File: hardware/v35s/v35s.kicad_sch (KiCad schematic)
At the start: 13 parts, among them J1 nuMezzanine_4x34, U1 uPD70337L-8-xxx

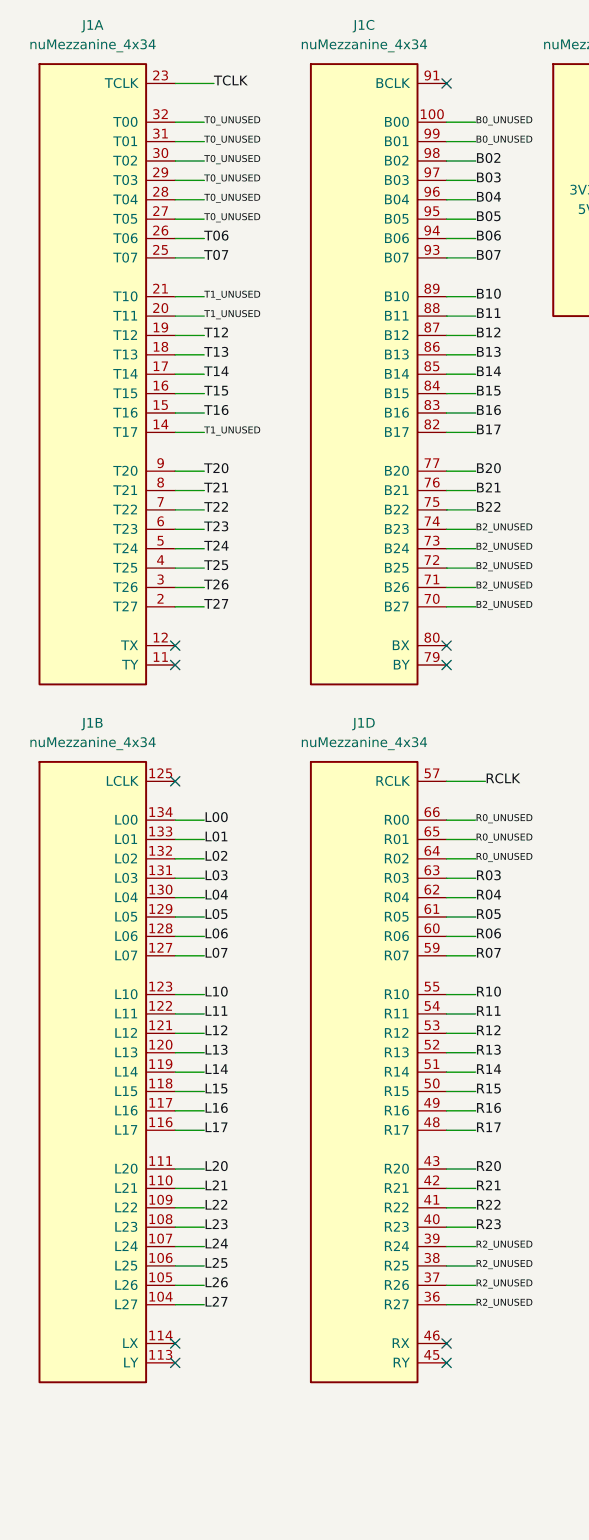
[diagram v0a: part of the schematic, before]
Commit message: Update mainboard to revision 2
Add an additional 8 bidirectional channels
Replace SPI PSRAM with hyperram
Remove LEDs
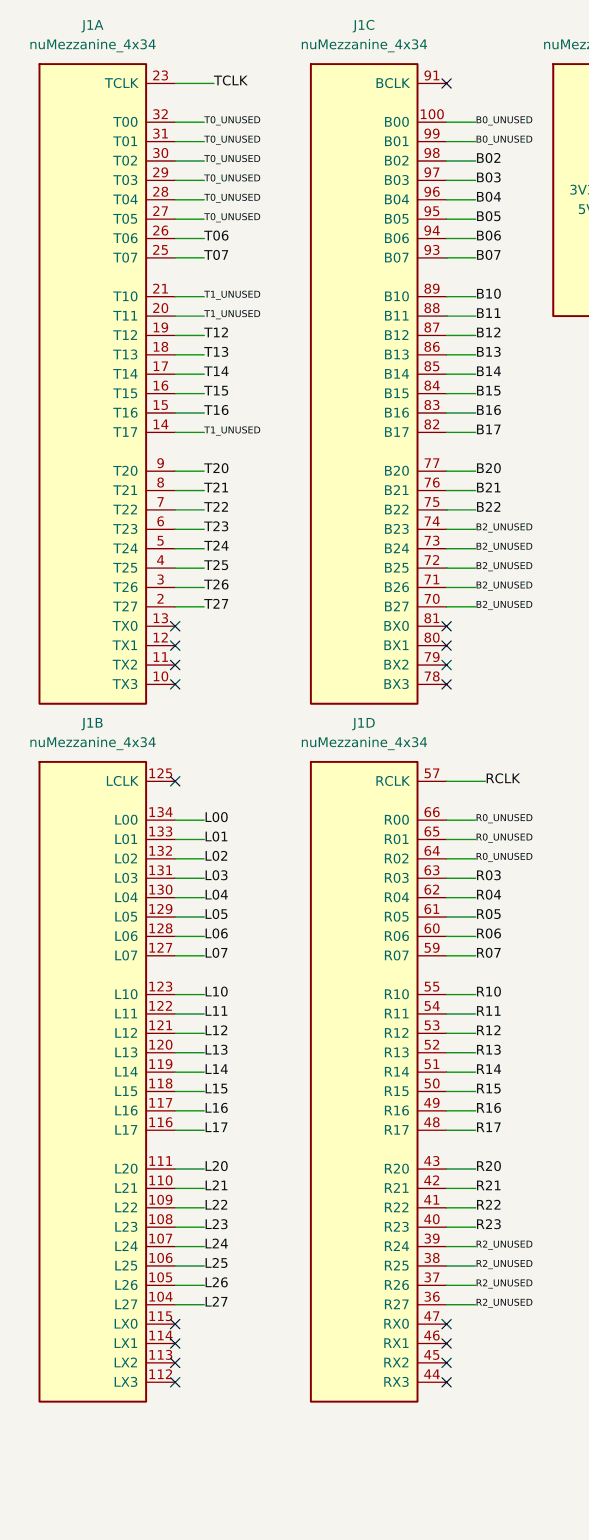
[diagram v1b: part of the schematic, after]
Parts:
- C1, C2, C3: footprint Capacitor_THT:C_Disc_D5.0mm_W2.5mm_P5.00mm -> Capacitor_SMD:C_0805_2012Metric_Pad1.18x1.45mm_HandSolder
- R1, R2, R3, R4, R5, R6, R7, R8: footprint Resistor_THT:R_Axial_DIN0207_L6.3mm_D2.5mm_P7.62mm_Horizontal -> Resistor_SMD:R_0805_2012Metric_Pad1.20x1.40mm_HandSolder
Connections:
- net GND: now also J1.102 (GND), J1.136 (GND); no longer J1.10 (GND), J1.112 (GND), J1.115 (GND), J1.13 (GND), J1.44 (GND), J1.47 (GND), J1.78 (GND), J1.81 (GND)
- no-connect marks 14 -> 22
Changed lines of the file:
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@@
           (size 1.27 1.27))
         (justify left)))
-    (property "Footprint" "Capacitor_THT:C_Disc_D5.0mm_W2.5mm_P5.00mm"
+    (property "Footprint" "Capacitor_SMD:C_0805_2012Metric_Pad1.18x1.45mm_HandSolder"
       (at 383.54 243.84 0)
       (effects
@@
           (size 1.27 1.27))
         (justify left)))
-    (property "Footprint" "Capacitor_THT:C_Disc_D5.0mm_W2.5mm_P5.00mm"
+    (property "Footprint" "Capacitor_SMD:C_0805_2012Metric_Pad1.18x1.45mm_HandSolder"
       (at 416.56 243.84 0)
       (effects
@@
           (size 1.27 1.27))
         (justify left)))
-    (property "Footprint" "Capacitor_THT:C_Disc_D5.0mm_W2.5mm_P5.00mm"
+    (property "Footprint" "Capacitor_SMD:C_0805_2012Metric_Pad1.18x1.45mm_HandSolder"
       (at 449.58 243.84 0)
       (effects
@@
           (size 1.27 1.27))
         (justify left)))
-    (property "Footprint" "Resistor_THT:R_Axial_DIN0207_L6.3mm_D2.5mm_P7.62mm_Horizontal"
+    (property "Footprint" "Resistor_SMD:R_0805_2012Metric_Pad1.20x1.40mm_HandSolder"
       (at 391.16 302.26 0)
       (effects
@@
           (size 1.27 1.27))
         (justify left)))
-    (property "Footprint" "Resistor_THT:R_Axial_DIN0207_L6.3mm_D2.5mm_P7.62mm_Horizontal"
+    (property "Footprint" "Resistor_SMD:R_0805_2012Metric_Pad1.20x1.40mm_HandSolder"
       (at 454.66 302.26 0)
       (effects
@@
           (size 1.0 1.0))
         (justify left)))
-    (property "Footprint" "Resistor_THT:R_Axial_DIN0207_L6.3mm_D2.5mm_P7.62mm_Horizontal"
+    (property "Footprint" "Resistor_SMD:R_0805_2012Metric_Pad1.20x1.40mm_HandSolder"
       (at 91.44 373.38 0)
       (effects
@@
           (size 1.0 1.0))
         (justify left)))
-    (property "Footprint" "Resistor_THT:R_Axial_DIN0207_L6.3mm_D2.5mm_P7.62mm_Horizontal"
+    (property "Footprint" "Resistor_SMD:R_0805_2012Metric_Pad1.20x1.40mm_HandSolder"
       (at 147.32 373.38 0)
       (effects
@@
           (size 1.0 1.0))
         (justify left)))
-    (property "Footprint" "Resistor_THT:R_Axial_DIN0207_L6.3mm_D2.5mm_P7.62mm_Horizontal"
+    (property "Footprint" "Resistor_SMD:R_0805_2012Metric_Pad1.20x1.40mm_HandSolder"
       (at 203.2 373.38 0)
       (effects
@@
           (size 1.0 1.0))
         (justify left)))
-    (property "Footprint" "Resistor_THT:R_Axial_DIN0207_L6.3mm_D2.5mm_P7.62mm_Horizontal"
+    (property "Footprint" "Resistor_SMD:R_0805_2012Metric_Pad1.20x1.40mm_HandSolder"
       (at 259.08 373.38 0)
       (effects
@@
           (size 1.0 1.0))
         (justify left)))
-    (property "Footprint" "Resistor_THT:R_Axial_DIN0207_L6.3mm_D2.5mm_P7.62mm_Horizontal"
+    (property "Footprint" "Resistor_SMD:R_0805_2012Metric_Pad1.20x1.40mm_HandSolder"
       (at 314.96 373.38 0)
       (effects
@@
           (size 1.0 1.0))
         (justify left)))
-    (property "Footprint" "Resistor_THT:R_Axial_DIN0207_L6.3mm_D2.5mm_P7.62mm_Horizontal"
+    (property "Footprint" "Resistor_SMD:R_0805_2012Metric_Pad1.20x1.40mm_HandSolder"
       (at 370.84 373.38 0)
       (effects
@@
       (font
         (size 1.1 1.1)))
-))
+)(no_connect (at 36.83 186.69))
+(no_connect (at 36.83 194.31))
+(no_connect (at 36.83 95.25))
+(no_connect (at 36.83 102.87))
+(no_connect (at 72.39 186.69))
+(no_connect (at 72.39 194.31))
+(no_connect (at 72.39 95.25))
+(no_connect (at 72.39 102.87))
+)
